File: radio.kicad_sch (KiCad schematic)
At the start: 24 parts, among them IC5 S2-LPQTR, IC6 BALF-SPI2-01D3, Y3 NX1612SA-50M-EXS00A-CS08403

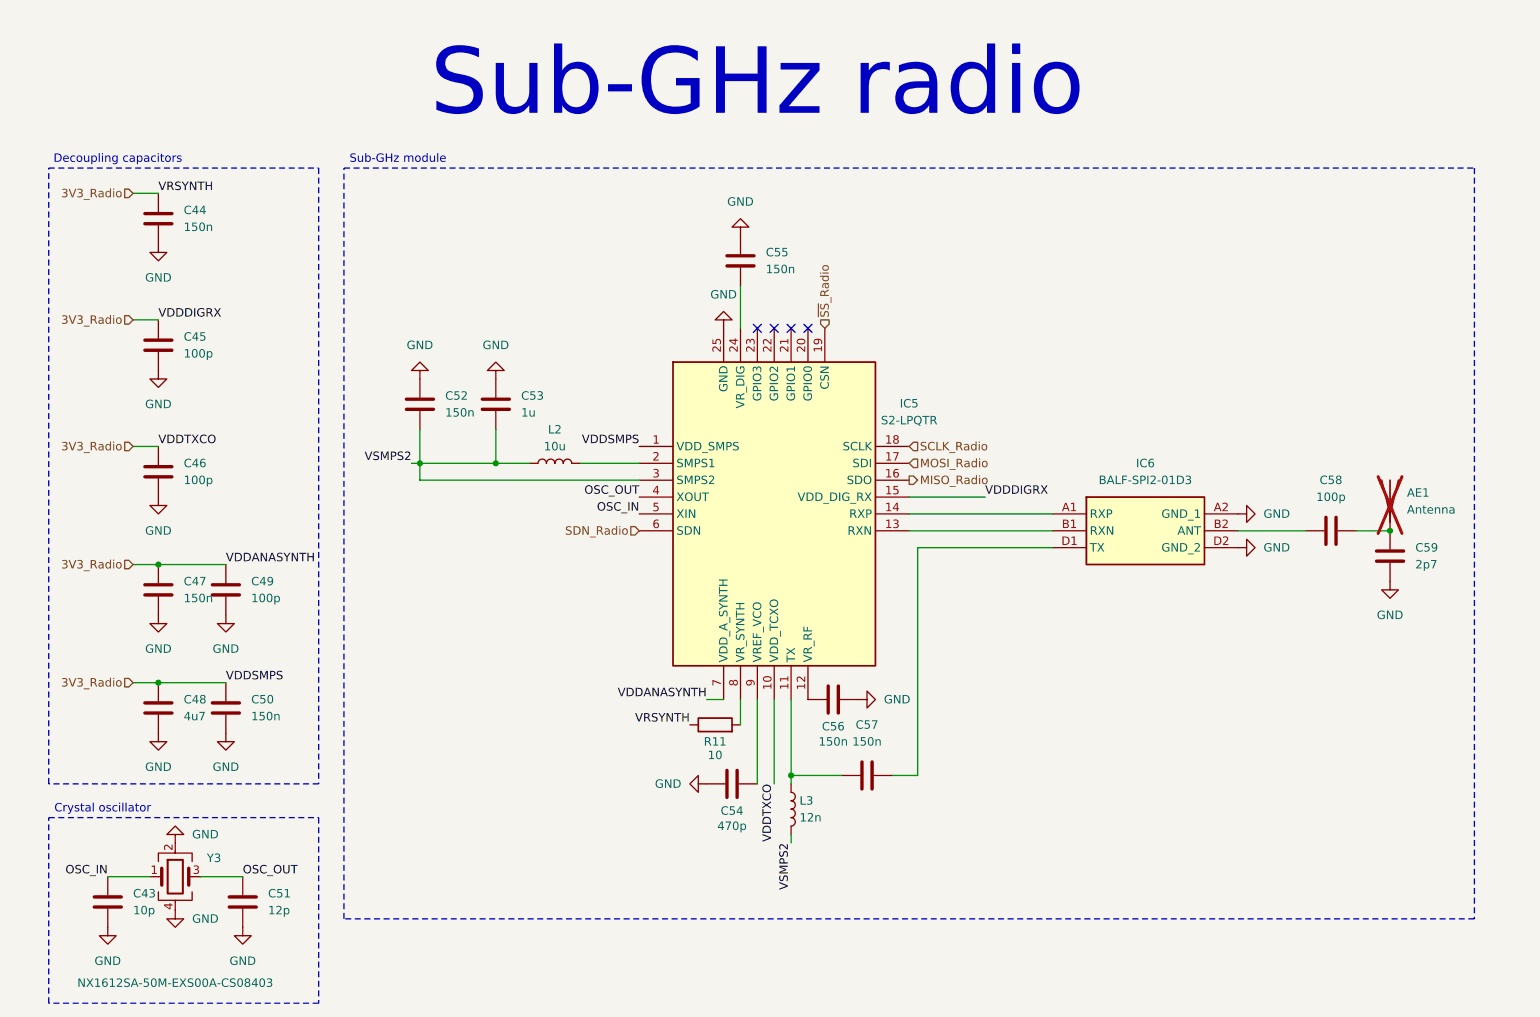
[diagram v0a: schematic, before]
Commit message: Fiw warnings concerning multiple name for the same label
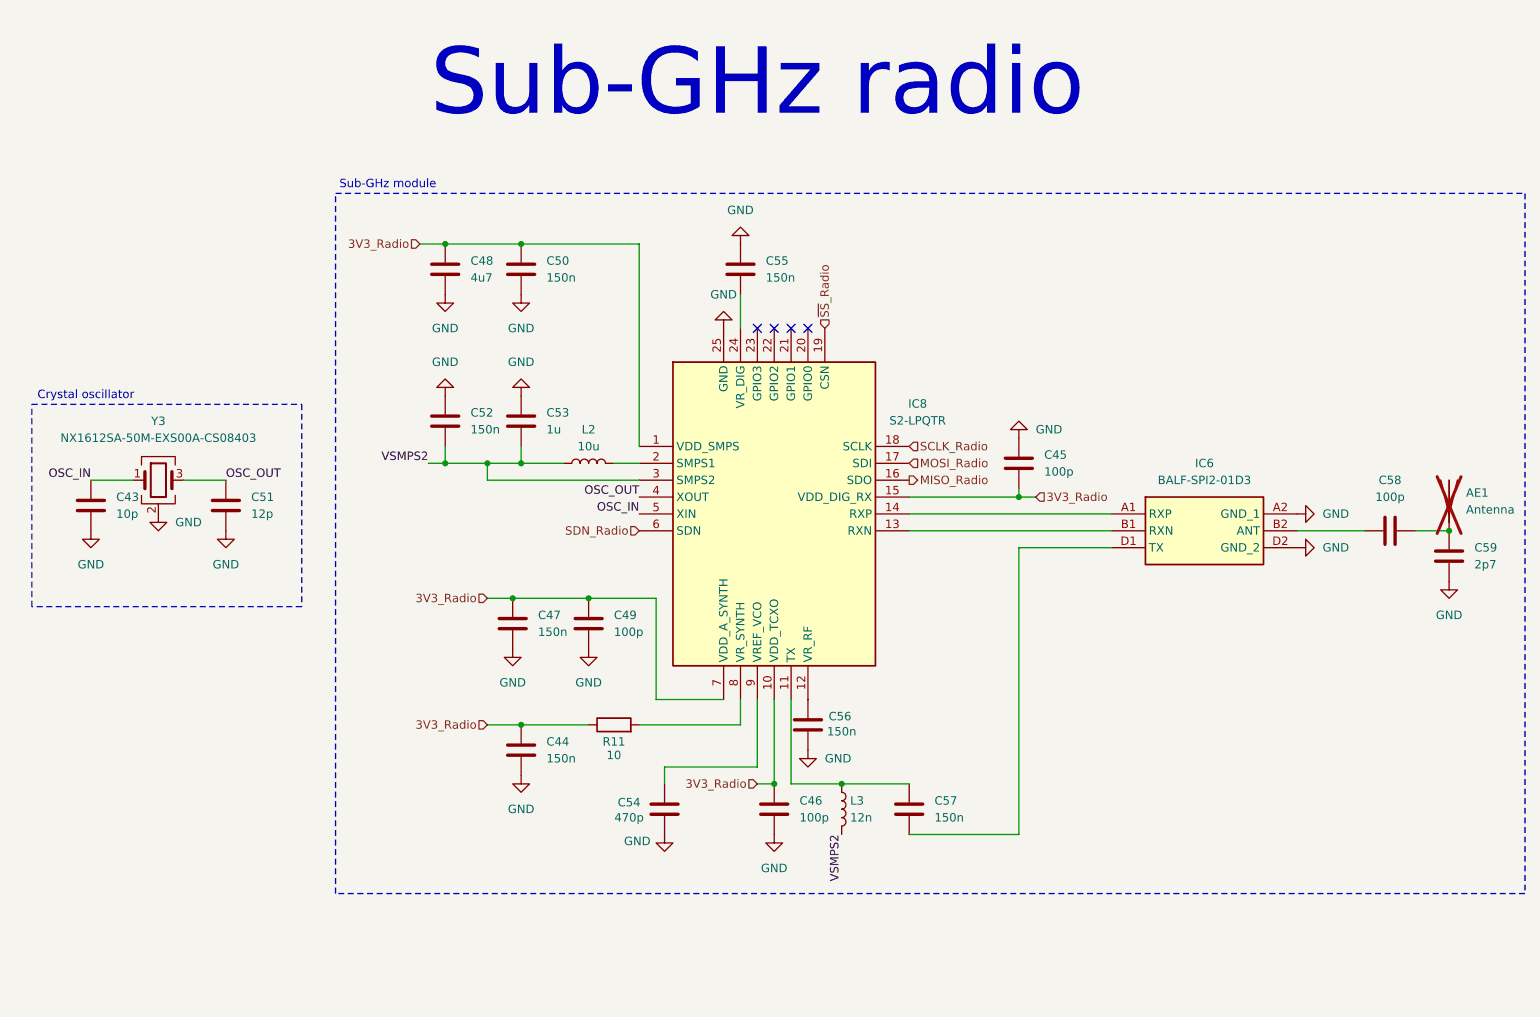
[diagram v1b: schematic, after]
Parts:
- removed IC5: S2-LPQTR, weather-station-poc-fp:QFN50P400X400X100-25N-D, symbol weather-station-poc-sym:S2-LPQTR
- added IC8: S2-LPQTR, weather-station-poc-fp:QFN50P400X400X100-25N-D, symbol weather-station-poc-sym:S2-LPQTR
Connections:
- net 3V3_Radio: now also C45.2, IC8.1 (VDD_SMPS), IC8.10 (VDD_TCXO), IC8.15 (VDD_DIG_RX), IC8.7 (VDD_A_SYNTH); no longer C45.1
- net GND: now also C45.1, C56.1, IC8.25 (GND); no longer C45.2, C56.2
- net MISO_Radio: now also IC8.16 (SDO)
- net MOSI_Radio: now also IC8.17 (SDI)
- net OSC_IN: now also IC8.5 (XIN)
- net OSC_OUT: now also IC8.4 (XOUT)
- net SCLK_Radio: now also IC8.18 (SCLK)
- net SDN_Radio: now also IC8.6 (SDN)
- net VSMPS2: now also IC8.3 (SMPS2)
- net ~{SS}_Radio: now also IC8.19 (CSN)
- net at C55.1: now also IC8.24 (VR_DIG)
- net at C54.2: now also IC8.9 (VREF_VCO)
- net at L3.1: now also C57.2, IC8.11 (TX); no longer C57.1
- net at IC6.D1 (TX): now also C57.1; no longer C57.2
- net at IC6.A1 (RXP): now also IC8.14 (RXP)
- net at IC6.B1 (RXN): now also IC8.13 (RXN)
- net at R11.2: now also IC8.8 (VR_SYNTH)
- net at L2.2: now also IC8.2 (SMPS1)
- new net: C56.2, IC8.12 (VR_RF)
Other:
- note removed: "Decoupling capacitors"
- moved on the sheet: AE1, C43, C44, C45, C46, C47, C48, C49, C50, C51, C52, C53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

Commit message: Move SWD debug connector from debug sheet to MCU sheet
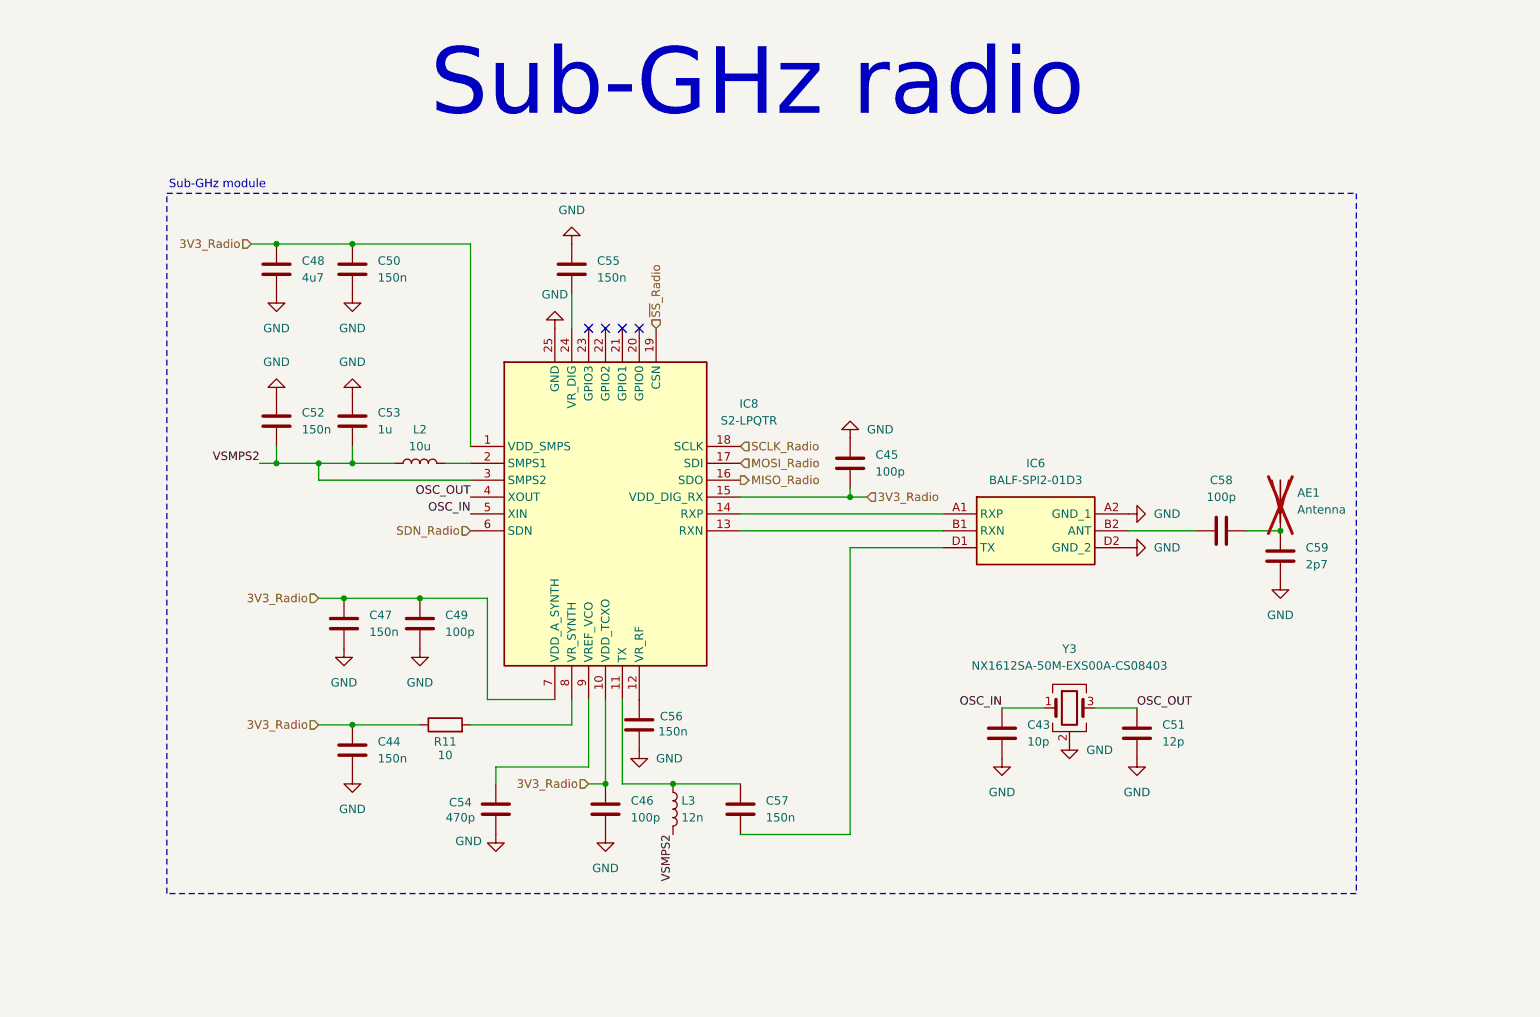
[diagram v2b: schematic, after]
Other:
- note removed: "Crystal oscillator"
- moved on the sheet: AE1, C43, C44, C45, C46, C47, C48, C49, C50, C51, C52, C53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

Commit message: Reset components indexing
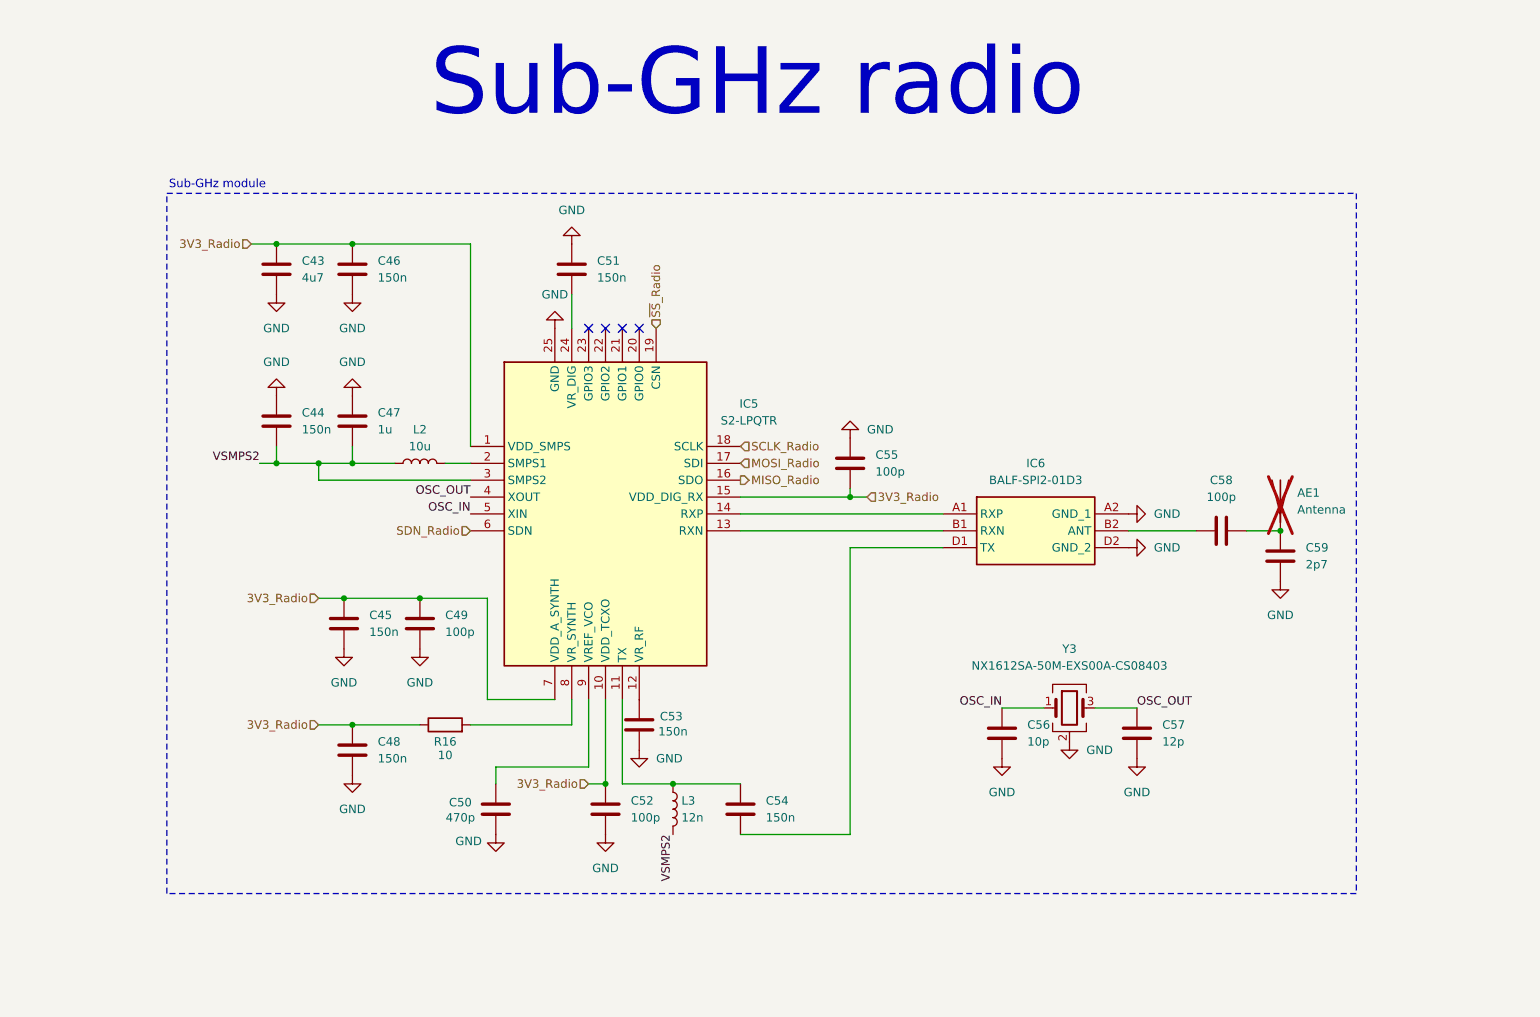
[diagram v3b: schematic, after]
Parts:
- renumbered C48 to C43, C52 to C44, C47 to C45, C50 to C46, C53 to C47, C44 to C48, C54 to C50, C55 to C51, C46 to C52, C56 to C53, C57 to C54, C45 to C55, C43 to C56, C51 to C57, IC8 to IC5, R11 to R16
